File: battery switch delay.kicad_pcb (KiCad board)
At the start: 2 copper layers, 40 x 56 mm, 15 parts, among them J1 5mm pitch 4 position screw te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, K1 FINDER-36.11, Q1 Q_NPN, U2 MIC2920A-12WS-TR_SOT223

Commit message: barely anything
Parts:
- moved R2 1.58 mm to (114.2, 109.3), turned to 0 degrees
- moved D1 0.79 mm to (119.0, 109.4), turned to 0 degrees
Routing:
- net Net-(A1-D2): track 33.0 -> 37.0 mm

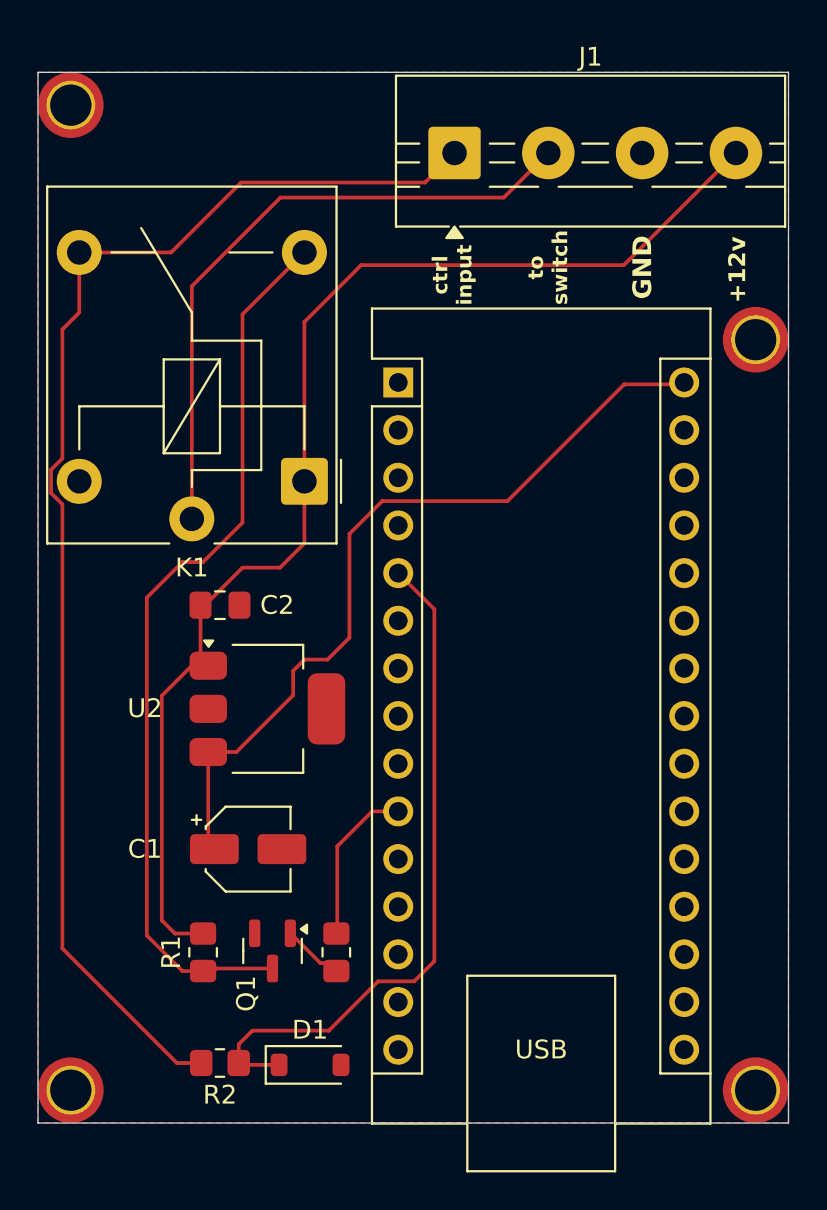
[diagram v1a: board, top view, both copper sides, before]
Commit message: added qr code and text to the repo
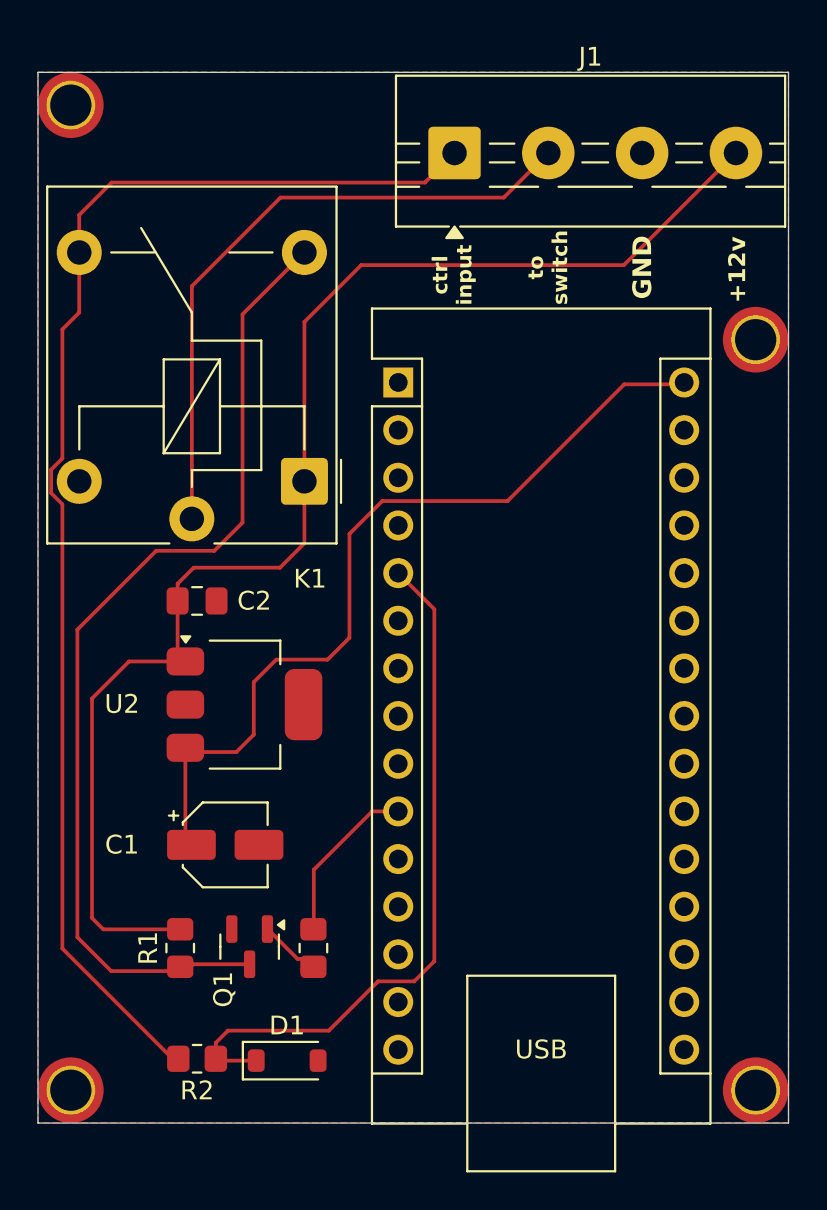
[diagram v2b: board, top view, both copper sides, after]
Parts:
- added G***: LOGO, LOGO, B.Cu at (131.3, 69.1)
- moved C1 1.24 mm to (114.5, 97.7)
- moved C2 1.24 mm to (113.0, 84.7)
- moved D1 1.24 mm to (117.8, 109.2)
- moved Q1 1.24 mm to (115.8, 103.1)
- moved R1 1.24 mm to (112.1, 103.2)
- moved R2 1.24 mm to (113.0, 109.1)
- moved R3 1.24 mm to (119.2, 103.2)
- moved U2 1.24 mm to (115.5, 90.2)
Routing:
- net +12V: track 67.1 -> 72.9 mm
- net Net-(Q1-C): track 48.2 -> 53.5 mm
- net Net-(A1-VIN): track 43.1 -> 45.3 mm
- net Net-(A1-D2): track 37.0 -> 38.0 mm

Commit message: fixed ground pour to include the relay
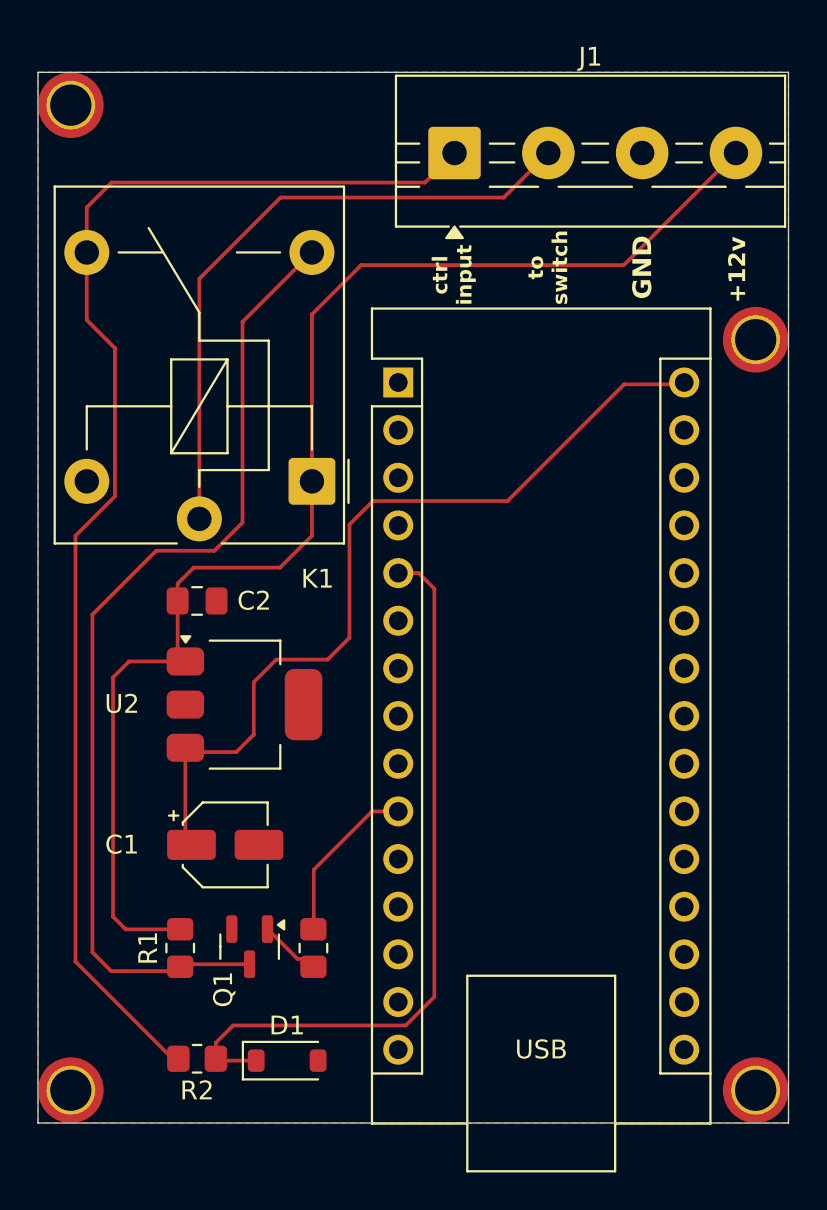
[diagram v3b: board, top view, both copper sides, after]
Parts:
- moved K1 0.40 mm to (119.1, 78.3)
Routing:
- net Net-(A1-D2): track 38.0 -> 39.8 mm
- net +12V: track 72.9 -> 71.7 mm
- net ctrl: track 69.9 -> 70.6 mm
